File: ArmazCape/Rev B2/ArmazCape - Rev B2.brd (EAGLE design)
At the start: 85 x 70.5 mm, 160 parts, among them J2 85505-5113, Q1 32.768kHz, 12.5pF, Q2 ASE, Q4 IRLML6344TRPBF, Q5 IRLML6344TRPBF, U1 L7985A, U12 24AA256-I/SN, U13 L7985A, U4 DS1307ZN+, U5 CD4050BD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

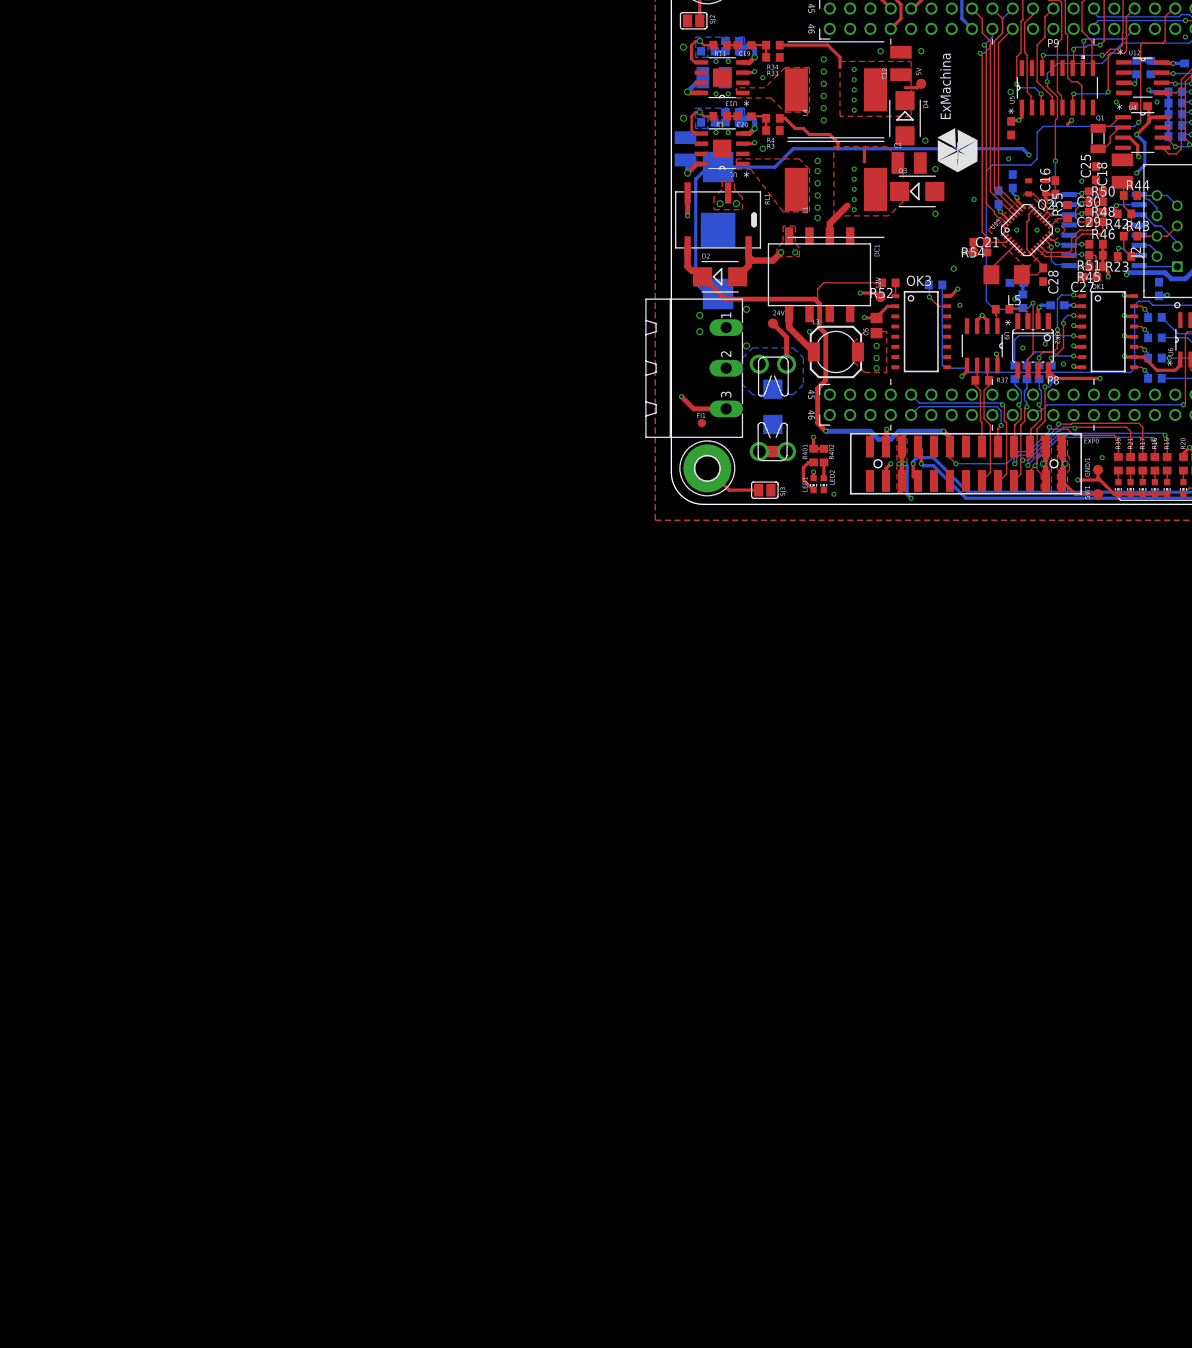
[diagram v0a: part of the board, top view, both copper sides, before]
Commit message: Repaired ArmazCape - Rev B2
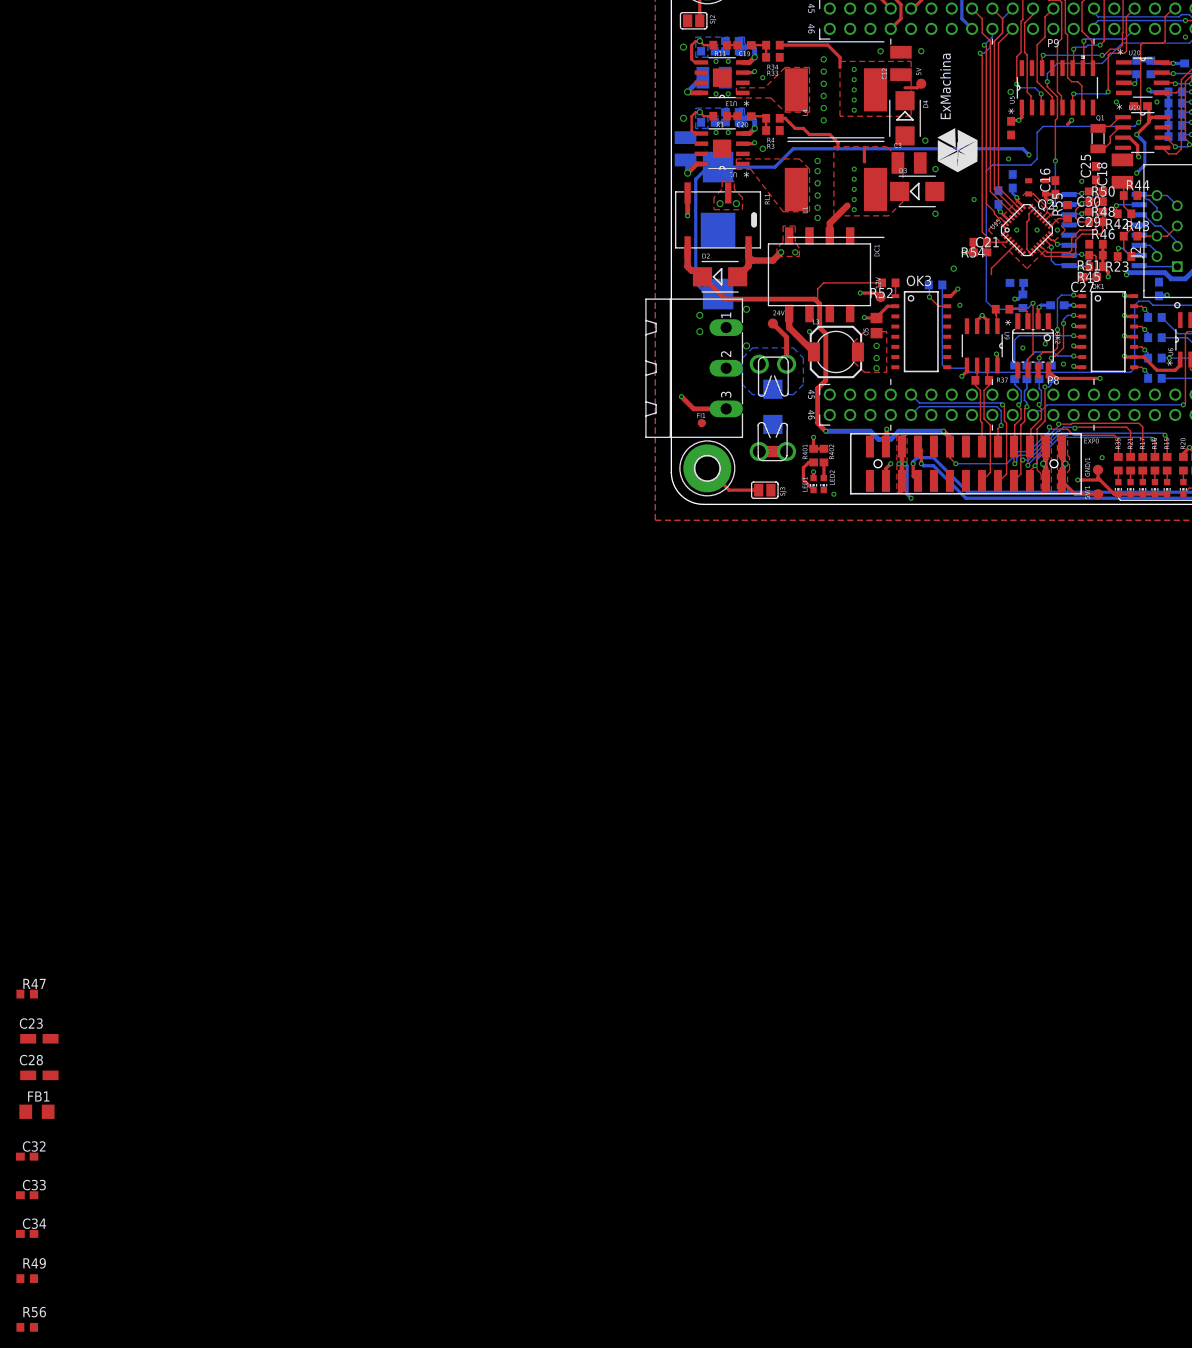
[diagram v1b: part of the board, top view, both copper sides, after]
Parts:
- removed L5: 1uH, rcl:L4532M
- removed U12: 24AA256-I/SN, Microchip_By_element14_Batch_1:SOIC127P600X175-8N
- removed U4: DS1307ZN+, maxim:SOIC127P600X175-8N
- added C23: 4.7uF, rcl:CT3216
- added C32, C33, C34: 0.1uF, rcl:C0603
- added FB1: HI1206N101R-10, emi_filter:1206
- added R47: 4.7K, rcl:R0603
- added R49, R56: 1k, rcl-2:R0603
- added U19: DS1307ZN+, ArmazCape - Rev B2:MAXIM_SOIC127P600X175-8N
- added U20: 24AA256-I/SN, ArmazCape - Rev B2:MICROCHIP_BY_ELEMENT14_BATCH_1_SOIC127P600X175-8N
- C28: value 0.1uF -> 4.7uF; device rcl:C0603 -> rcl:CT3216
- moved C28 160.5 mm to (-79.0, -71.4), turned to 0 degrees
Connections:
- removed net TD+: R45.2, U$4.1, U$5.14
- removed net TD-: R46.1, U$4.3, U$5.15
- new net N$4200: R45.2, U$4.3, U$5.14
- new net N$4400: R46.1, U$4.1, U$5.15
- new net VDD18PLL: C28.+, C32.1, C33.1, FB1.2, U$5.23, U$5.9
- net +3V3: now also Q2.1, U20.8; no longer U12.8
- net +5V: now also U19.8; no longer U4.8
- net +5V/1: now also C34.1, R56.1
- net DMX0-A: now also R49.1
- net DMX0-B: now also R56.2
- net GND: now also C23.-, C28.-, C32.2, C33.2, R47.1, U19.4, U20.1, U20.2, U20.4; no longer C28.2, U12.1, U12.2, U12.4, U4.4
- net GND1: now also C34.2, R49.2
- net I2C2_SCL: now also U19.6, U20.6; no longer U12.6, U4.6
- net I2C2_SDA: now also U19.5, U20.5; no longer U12.5, U4.5
- net N$24: now also U19.1; no longer U4.1
- net N$26: now also U19.2; no longer U4.2
- net N$34: now also U20.7; no longer U12.7
- net N$35: now also U20.3; no longer U12.3
- net N$4: now also C30.2, U$4.6; no longer L5.2, U$5.5
- net N$51: now also U$4.8; no longer U$4.6
- net N$52: now also R47.2, U$5.6; no longer C30.2, U$4.8
- net VBAT+: now also U19.3; no longer U4.3
- net VDD18CORE: now also C23.+, FB1.1, U$5.5; no longer C28.1, L5.1, U$5.23, U$5.9
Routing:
- net TD+: track 8.07 -> 0.00 mm, vias 2 -> 0
- net N$4200: track 0.00 -> 7.71 mm, vias 0 -> 2
- net VDD18CORE: track 11.6 -> 4.91 mm
- net VDD18PLL: track 0.00 -> 6.06 mm
- net TD-: track 5.70 -> 0.00 mm, vias 2 -> 0
- net N$4: track 4.91 -> 0.00 mm
- net N$4400: track 0.00 -> 2.95 mm, vias 0 -> 1
- net N$52: track 2.68 -> 0.00 mm, vias 1 -> 0
- net N$51: track 2.68 -> 4.17 mm, vias 1 -> 2

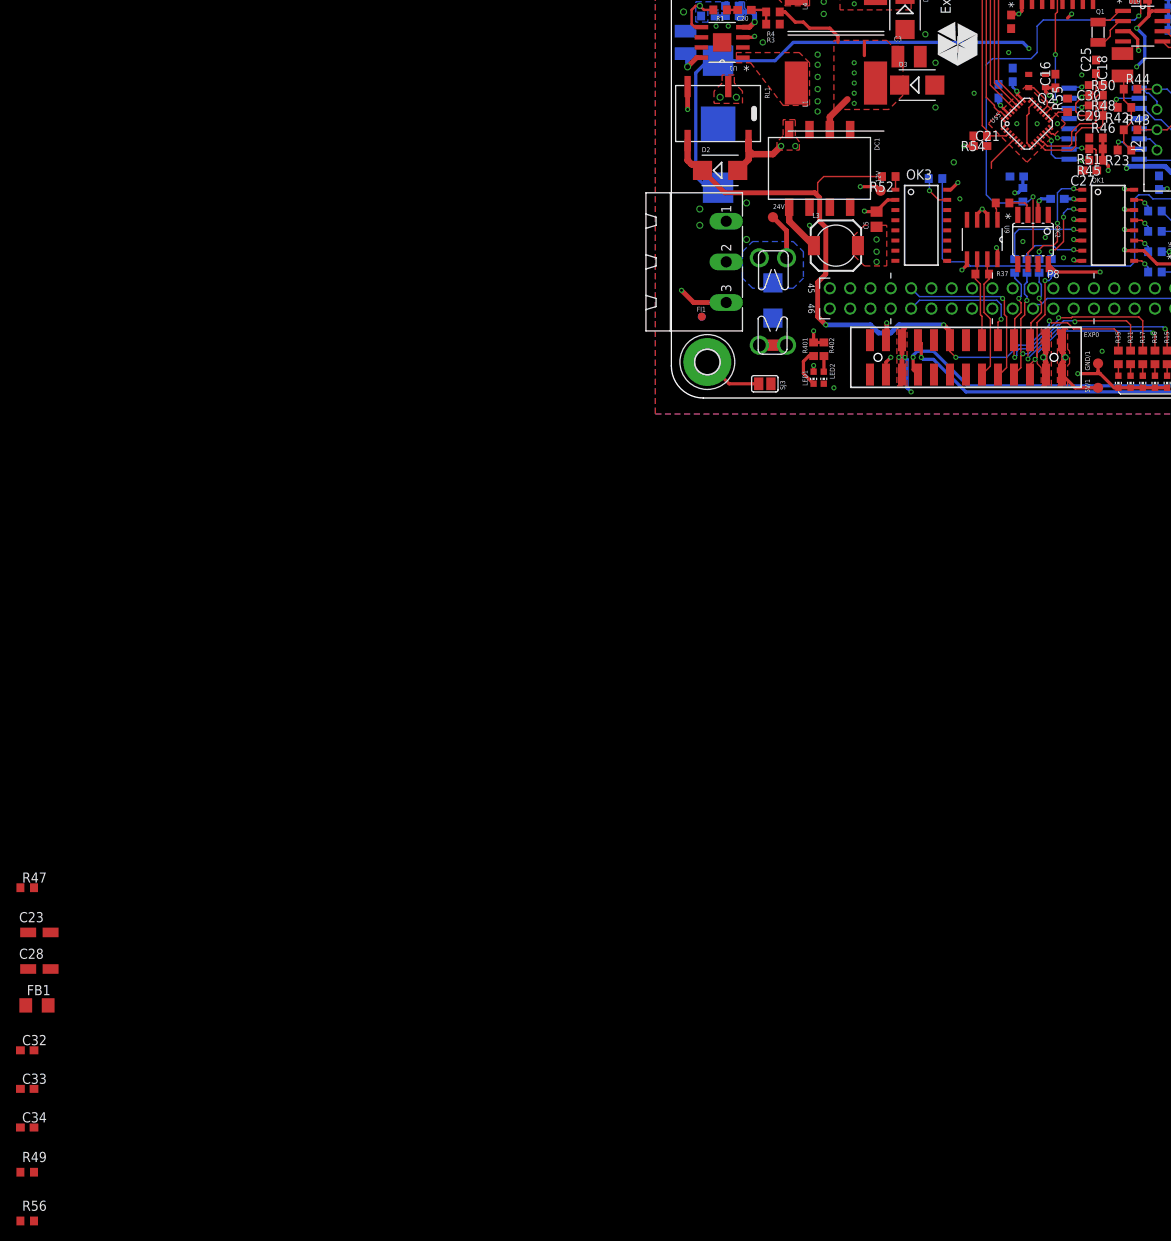
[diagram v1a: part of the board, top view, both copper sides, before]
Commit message: Updated routed board - ArmazCape - Rev B2 This version doesn't provide isolated +5v; must be supplied via ArmazConnect
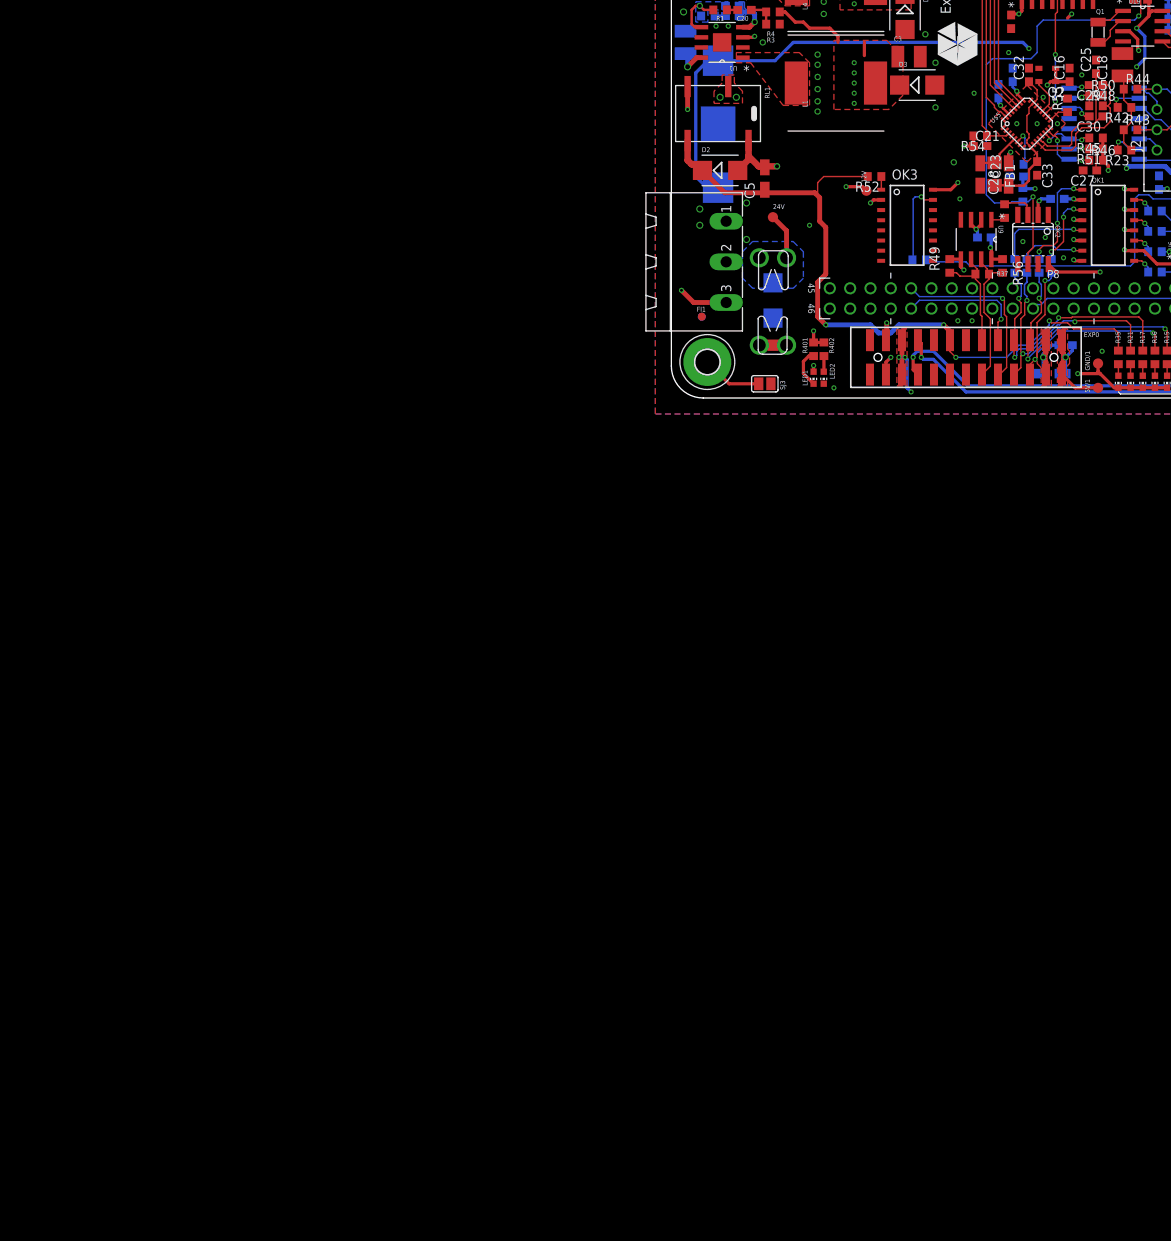
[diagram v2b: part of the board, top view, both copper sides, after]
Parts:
- removed DC1: NTE1205MC, dc-dc-converter:NTE
- removed L3: 1uH, resistor-epcos:B82462G4
- added C35: 0.1uF, rcl:C0603
- added C36: 4.7uF, rcl:CT3216
- C5: device rcl:C0805 -> rcl:CT3216
- moved U$3 227.7 mm to (110.7, 65.0)
- moved C32 174.8 mm to (44.7, 40.4), turned to 90 degrees
- moved C33 170.8 mm to (45.7, 28.7), turned to 270 degrees
- moved R56 170.6 mm to (41.4, 16.5), turned to 270 degrees
- moved C34 163.4 mm to (39.1, 20.1), flipped to the bottom
- moved R49 161.7 mm to (34.8, 16.5), turned to 90 degrees
- moved FB1 158.4 mm to (40.4, 27.9), turned to 270 degrees
- moved C28 156.7 mm to (42.2, 27.9), turned to 90 degrees
- moved R47 153.2 mm to (43.2, 29.2), flipped to the bottom, turned to 180 degrees
- moved C23 151.0 mm to (38.6, 27.9), turned to 270 degrees
- moved C5 14.9 mm to (11.7, 27.4)
- moved R53 10.4 mm to (31.0, 17.3)
- moved C30 3.91 mm to (53.1, 35.2)
- moved R45 2.79 mm to (53.1, 32.5)
- moved R46 2.79 mm to (53.1, 29.7)
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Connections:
- removed net N$21: DC1.8, L3.1
- net +12V: no longer DC1.3
- net +5V/1: now also C35.1, C36.+; no longer C5.1, L3.2
- net DV0: now also C5.+
- net GND: no longer DC1.1
- net GND1: now also C35.2, C36.-, C5.-; no longer C5.2, DC1.7
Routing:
- net GND1: track 48.5 -> 64.0 mm, vias 11 -> 10
- net VDD18PLL: track 6.06 -> 19.0 mm
- net SW_EXT4_IN: track 56.6 -> 48.6 mm
- net +5V/1: track 14.5 -> 21.3 mm, vias 6 -> 3
- net N$54: track 4.26 -> 10.4 mm
- net N$21: track 6.11 -> 0.00 mm
- net N$4400: track 2.95 -> 7.94 mm, vias 1 -> 2
- net N$2000: track 13.4 -> 18.3 mm
- net N$52: track 0.00 -> 4.72 mm, vias 0 -> 1
- net +12V: track 70.5 -> 65.8 mm
- net +3V3: track 134.7 -> 139.0 mm
- net DMX0-A: track 10.5 -> 14.4 mm
- net N$4: track 0.00 -> 3.33 mm, vias 0 -> 1
- net N$50: track 9.93 -> 7.26 mm
- net DMX0-B: track 15.5 -> 17.6 mm
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
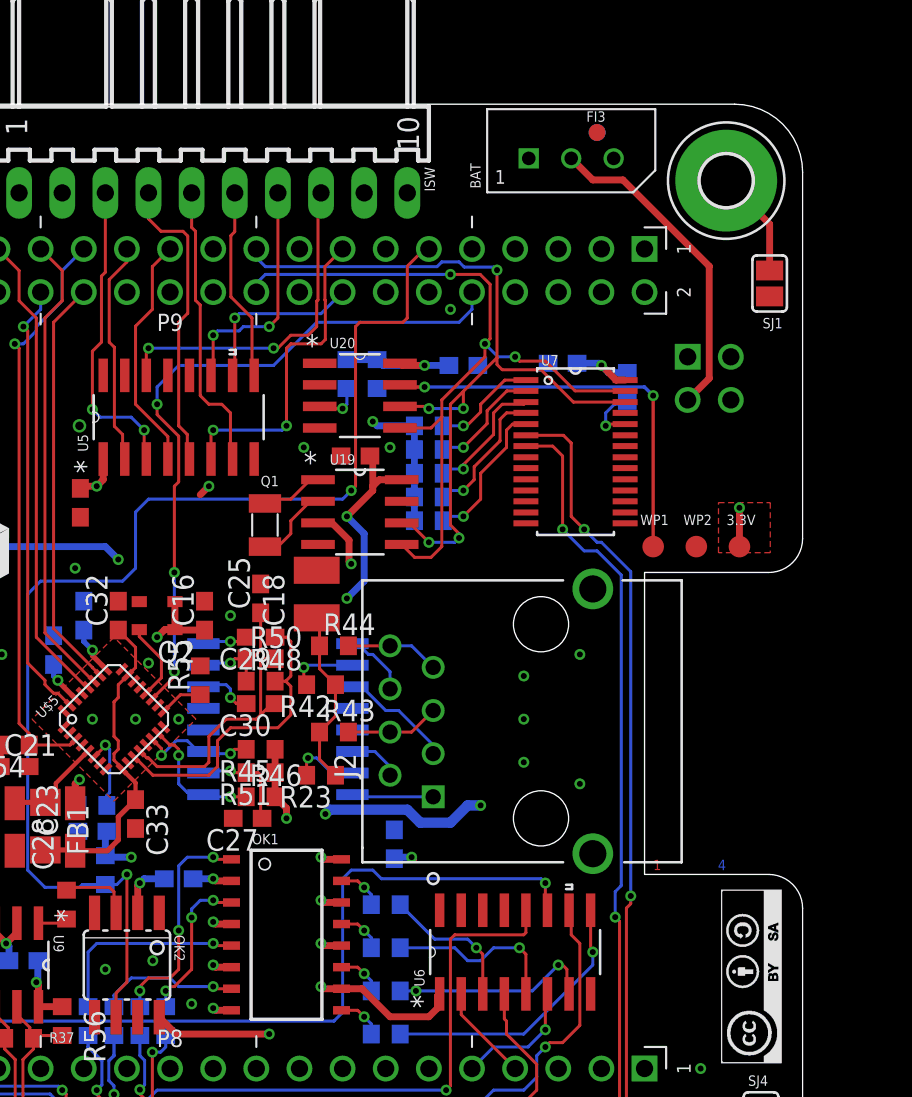
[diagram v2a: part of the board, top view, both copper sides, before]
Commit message: Added isolation around RJ45 connector
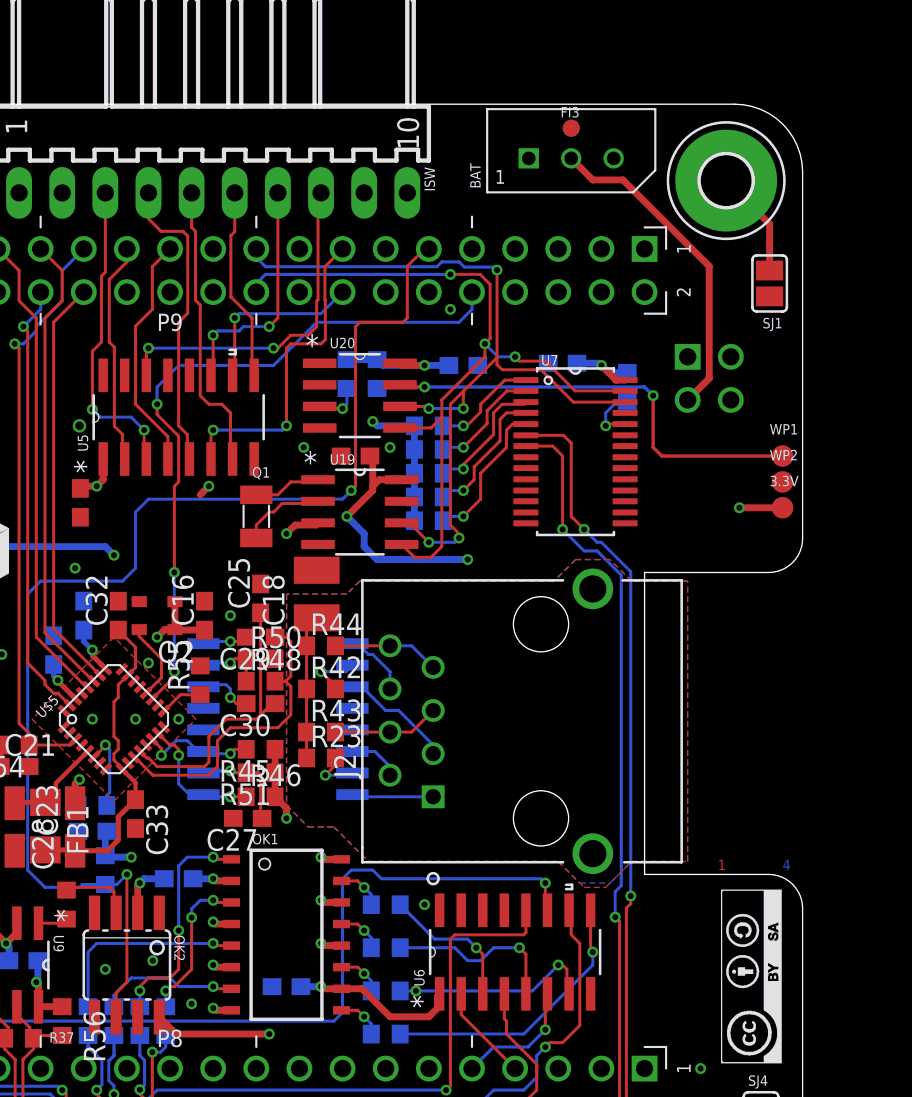
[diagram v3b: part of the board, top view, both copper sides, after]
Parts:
- moved C10 10.5 mm to (54.6, 18.5), turned to 0 degrees
- moved WP1 9.30 mm to (83.8, 49.8)
- moved WP2 6.35 mm to (83.8, 48.3)
- moved 3.3V 3.42 mm to (83.8, 46.7)
- moved FI3 1.55 mm to (71.4, 69.1)
- moved FI7 1.55 mm to (71.4, 69.1)
- moved R23 1.02 mm to (56.6, 32.0), turned to 0 degrees
- moved R43 0.76 mm to (56.6, 33.5)
- moved R44 0.76 mm to (56.6, 38.6)
- moved Q1 0.72 mm to (52.8, 46.2)
- moved R42 0.25 mm to (56.6, 36.1), turned to 0 degrees
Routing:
- net +5V: track 48.9 -> 28.6 mm, vias 10 -> 8
- net VBAT+: track 77.6 -> 72.9 mm
- net N$48: track 10.5 -> 8.50 mm
- net N$34: track 26.9 -> 28.9 mm
- net N$44: track 4.03 -> 2.91 mm
- net N$47: track 5.52 -> 6.28 mm
- net N$46: track 5.52 -> 6.28 mm
- net N$45: track 4.00 -> 3.37 mm
- net +3V3: track 139.0 -> 139.2 mm, vias 20 -> 19
- net GND: vias 65 -> 61
